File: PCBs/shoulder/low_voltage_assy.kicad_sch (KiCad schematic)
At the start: 23 parts, among them J3 Conn_01x03, U3 LM317_TO-220, U4 LM317_TO-220

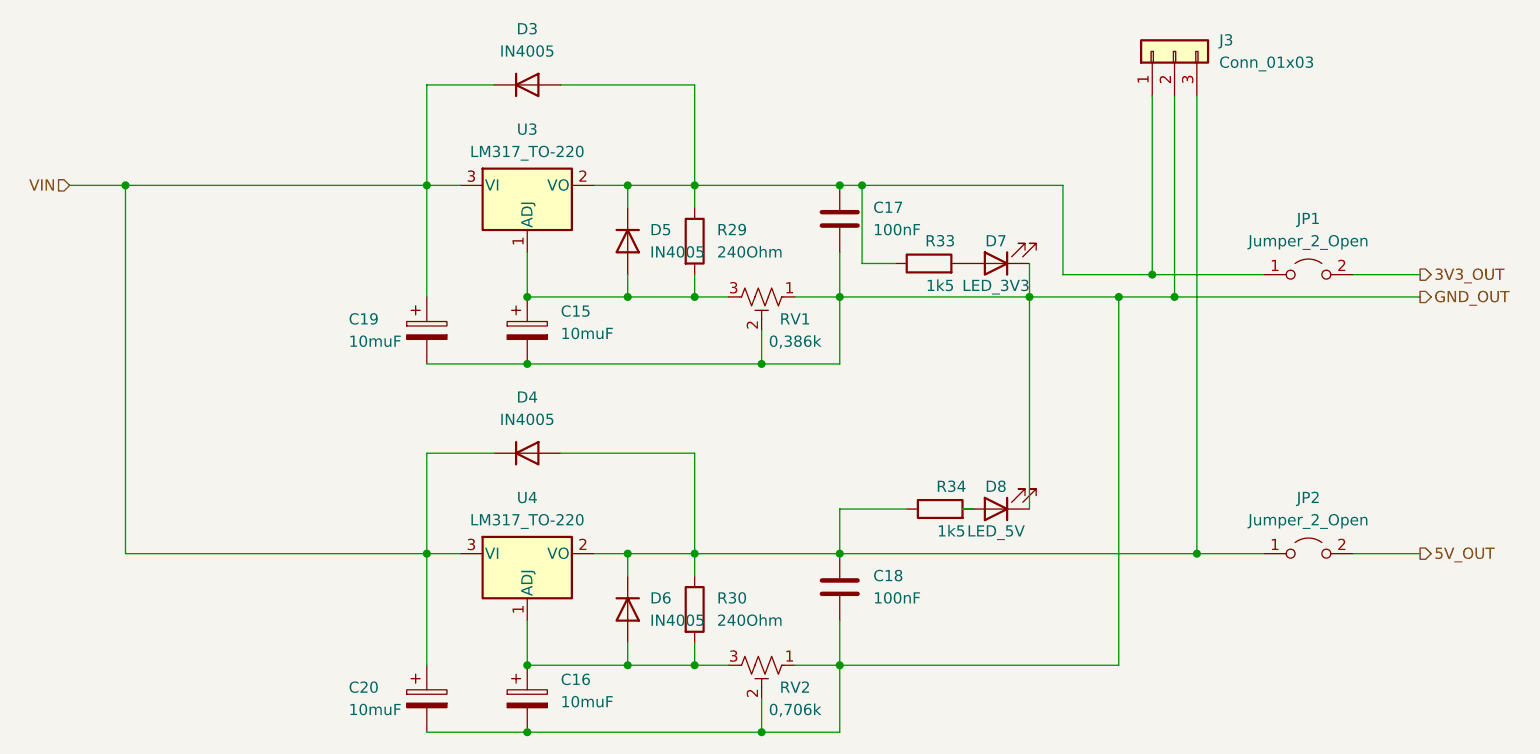
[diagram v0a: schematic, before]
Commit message: merged changes from timertests, mostly documentation and such. Did not add tim6 config
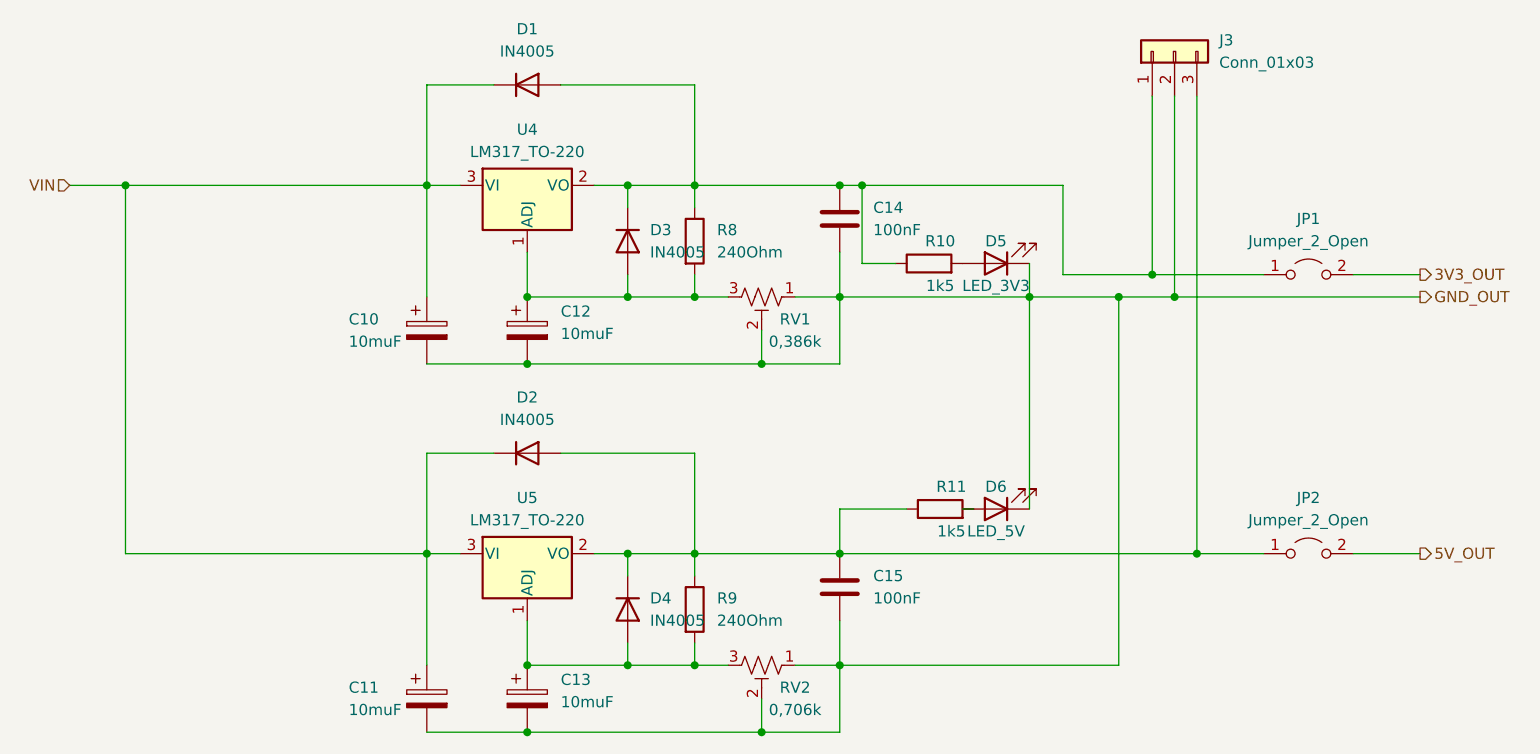
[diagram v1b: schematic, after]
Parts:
- renumbered C19 to C10, C20 to C11, C15 to C12, C16 to C13, C17 to C14, C18 to C15, D3 to D1, D4 to D2, D5 to D3, D6 to D4, D7 to D5, D8 to D6, R33 to R10, R34 to R11, R29 to R8, R30 to R9, U3 to U4, U4 to U5
